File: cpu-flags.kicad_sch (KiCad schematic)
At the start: 10 parts, among them U44 74HCT02, U45 74HCT00, U9 74HCT173

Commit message: finished the control logic
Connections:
- no-connect marks 3 -> 5
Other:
- company: (none) -> TBR Designs
- title: (none) -> 8-bit CPU
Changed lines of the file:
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@@
 (kicad_sch (version 20230121) (generator eeschema)
   (paper "A4")
+  (title_block
+    (title "8-bit CPU")
+    (date "2023-11-28")
+    (rev "1.0")
+    (company "TBR Designs")
+  )
   (junction (at 135.89 132.08) (diameter 0) (color 0 0 0 0)
   )
@@
   (no_connect (at 201.93 100.33))
   (no_connect (at 199.39 100.33))
+  (no_connect (at 199.39 125.73))
+  (no_connect (at 201.93 125.73))
   (wire (pts (xy 142.24 87.63) (xy 181.61 87.63))
     (stroke (width 0) (type default) (color 255 0 0 1))

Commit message: redid the eeprom
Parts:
- renumbered D80 to D82, R127 to R125, U45 to U46, U44 to U47
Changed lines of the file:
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@@
   (symbol (lib_id "74xx:74HCT00") (at 125.73 95.25 0) (unit 3)
     (in_bom yes) (on_board yes) (dnp no) (fields_autoplaced)
-    (property "Reference" "U45" (at 125.7217 86.36 0)
+    (property "Reference" "U46" (at 125.7217 86.36 0)
       (effects (font (size 1.27 1.27)))
     )
@@
       (project "8-bit-cpu"
         (path "/100bb8d1-c3d6-4e1f-87b6-72e4e187243c/592ff0ed-0688-4db1-b04b-e905201025c7"
-          (reference "U45") (unit 3)
+          (reference "U46") (unit 3)
         )
       )
@@
   (symbol (lib_id "Device:R") (at 123.19 146.05 0) (unit 1)
     (in_bom yes) (on_board yes) (dnp no) (fields_autoplaced)
-    (property "Reference" "R127" (at 125.73 144.78 0)
+    (property "Reference" "R125" (at 125.73 144.78 0)
       (effects (font (size 1.27 1.27)) (justify left))
     )
@@
       (project "8-bit-cpu"
         (path "/100bb8d1-c3d6-4e1f-87b6-72e4e187243c/592ff0ed-0688-4db1-b04b-e905201025c7"
-          (reference "R127") (unit 1)
+          (reference "R125") (unit 1)
         )
       )
@@
         )
         (path "/100bb8d1-c3d6-4e1f-87b6-72e4e187243c/592ff0ed-0688-4db1-b04b-e905201025c7"
-          (reference "C53") (unit 1)
+          (reference "C54") (unit 1)
         )
       )
@@
         )
         (path "/100bb8d1-c3d6-4e1f-87b6-72e4e187243c/592ff0ed-0688-4db1-b04b-e905201025c7"
-          (reference "#PWR0191") (unit 1)
+          (reference "#PWR0189") (unit 1)
         )
       )
@@
   (symbol (lib_id "74xx:74HCT02") (at 67.31 72.39 0) (unit 1)
     (in_bom yes) (on_board yes) (dnp no) (fields_autoplaced)
-    (property "Reference" "U44" (at 67.31 63.5 0)
+    (property "Reference" "U47" (at 67.31 63.5 0)
       (effects (font (size 1.27 1.27)))
     )
@@
       (project "8-bit-cpu"
         (path "/100bb8d1-c3d6-4e1f-87b6-72e4e187243c/592ff0ed-0688-4db1-b04b-e905201025c7"
-          (reference "U44") (unit 1)
+          (reference "U47") (unit 1)
         )
       )
@@
         )
         (path "/100bb8d1-c3d6-4e1f-87b6-72e4e187243c/592ff0ed-0688-4db1-b04b-e905201025c7"
-          (reference "#PWR0194") (unit 1)
+          (reference "#PWR0192") (unit 1)
         )
       )
@@
   (symbol (lib_id "74xx:74HCT00") (at 237.49 41.91 0) (unit 5)
     (in_bom yes) (on_board yes) (dnp no) (fields_autoplaced)
-    (property "Reference" "U45" (at 243.84 40.64 0)
+    (property "Reference" "U46" (at 243.84 40.64 0)
       (effects (font (size 1.27 1.27)) (justify left))
     )
@@
       (project "8-bit-cpu"
         (path "/100bb8d1-c3d6-4e1f-87b6-72e4e187243c/592ff0ed-0688-4db1-b04b-e905201025c7"
-          (reference "U45") (unit 5)
+          (reference "U46") (unit 5)
         )
       )
@@
         )
         (path "/100bb8d1-c3d6-4e1f-87b6-72e4e187243c/592ff0ed-0688-4db1-b04b-e905201025c7"
-          (reference "#PWR0209") (unit 1)
+          (reference "#PWR0197") (unit 1)
         )
       )
@@
         )
         (path "/100bb8d1-c3d6-4e1f-87b6-72e4e187243c/592ff0ed-0688-4db1-b04b-e905201025c7"
-          (reference "#PWR0210") (unit 1)
+          (reference "#PWR0198") (unit 1)
         )
       )
@@
         )
         (path "/100bb8d1-c3d6-4e1f-87b6-72e4e187243c/592ff0ed-0688-4db1-b04b-e905201025c7"
-          (reference "C54") (unit 1)
+          (reference "C55") (unit 1)
         )
       )
@@
         )
         (path "/100bb8d1-c3d6-4e1f-87b6-72e4e187243c/592ff0ed-0688-4db1-b04b-e905201025c7"
-          (reference "#PWR0193") (unit 1)
+          (reference "#PWR0190") (unit 1)
         )
       )
@@
   (symbol (lib_id "Device:LED") (at 135.89 138.43 90) (unit 1)
     (in_bom yes) (on_board yes) (dnp no) (fields_autoplaced)
-    (property "Reference" "D80" (at 139.7 138.7475 90)
+    (property "Reference" "D82" (at 139.7 138.7475 90)
       (effects (font (size 1.27 1.27)) (justify right))
     )
@@
       (project "8-bit-cpu"
         (path "/100bb8d1-c3d6-4e1f-87b6-72e4e187243c/592ff0ed-0688-4db1-b04b-e905201025c7"
-          (reference "D80") (unit 1)
+          (reference "D82") (unit 1)
         )
       )
@@
   (symbol (lib_id "74xx:74HCT00") (at 96.52 80.01 0) (unit 1)
     (in_bom yes) (on_board yes) (dnp no) (fields_autoplaced)
-    (property "Reference" "U45" (at 96.5117 71.12 0)
+    (property "Reference" "U46" (at 96.5117 71.12 0)
       (effects (font (size 1.27 1.27)))
     )
@@
       (project "8-bit-cpu"
         (path "/100bb8d1-c3d6-4e1f-87b6-72e4e187243c/592ff0ed-0688-4db1-b04b-e905201025c7"
-          (reference "U45") (unit 1)
+          (reference "U46") (unit 1)
         )
       )
@@
         )
         (path "/100bb8d1-c3d6-4e1f-87b6-72e4e187243c/592ff0ed-0688-4db1-b04b-e905201025c7"
-          (reference "#PWR0196") (unit 1)
+          (reference "#PWR0195") (unit 1)
         )
       )
@@
         )
         (path "/100bb8d1-c3d6-4e1f-87b6-72e4e187243c/592ff0ed-0688-4db1-b04b-e905201025c7"
-          (reference "C58") (unit 1)
+          (reference "C56") (unit 1)
         )
       )
@@
   (symbol (lib_id "74xx:74HCT02") (at 67.31 87.63 0) (unit 2)
     (in_bom yes) (on_board yes) (dnp no) (fields_autoplaced)
-    (property "Reference" "U44" (at 67.31 78.74 0)
+    (property "Reference" "U47" (at 67.31 78.74 0)
       (effects (font (size 1.27 1.27)))
     )
@@
       (project "8-bit-cpu"
         (path "/100bb8d1-c3d6-4e1f-87b6-72e4e187243c/592ff0ed-0688-4db1-b04b-e905201025c7"
-          (reference "U44") (unit 2)
+          (reference "U47") (unit 2)
         )
       )
@@
   (symbol (lib_id "74xx:74HCT02") (at 67.31 102.87 0) (unit 3)
     (in_bom yes) (on_board yes) (dnp no) (fields_autoplaced)
-    (property "Reference" "U44" (at 67.31 93.98 0)
+    (property "Reference" "U47" (at 67.31 93.98 0)
       (effects (font (size 1.27 1.27)))
     )
@@
       (project "8-bit-cpu"
         (path "/100bb8d1-c3d6-4e1f-87b6-72e4e187243c/592ff0ed-0688-4db1-b04b-e905201025c7"
-          (reference "U44") (unit 3)
+          (reference "U47") (unit 3)
         )
       )
@@
         )
         (path "/100bb8d1-c3d6-4e1f-87b6-72e4e187243c/592ff0ed-0688-4db1-b04b-e905201025c7"
-          (reference "#PWR0195") (unit 1)
+          (reference "#PWR0194") (unit 1)
         )
       )
@@
   (symbol (lib_id "power:GND") (at 129.54 152.4 0) (unit 1)
     (in_bom yes) (on_board yes) (dnp no) (fields_autoplaced)
-    (property "Reference" "#PWR0190" (at 129.54 158.75 0)
+    (property "Reference" "#PWR0199" (at 129.54 158.75 0)
       (effects (font (size 1.27 1.27)) hide)
     )
@@
       (project "8-bit-cpu"
         (path "/100bb8d1-c3d6-4e1f-87b6-72e4e187243c/592ff0ed-0688-4db1-b04b-e905201025c7"
-          (reference "#PWR0190") (unit 1)
+          (reference "#PWR0199") (unit 1)
         )
       )
@@
         )
         (path "/100bb8d1-c3d6-4e1f-87b6-72e4e187243c/592ff0ed-0688-4db1-b04b-e905201025c7"
-          (reference "#PWR0192") (unit 1)
+          (reference "#PWR0191") (unit 1)
         )
       )
@@
   (symbol (lib_id "74xx:74HCT02") (at 265.43 41.91 0) (unit 5)
     (in_bom yes) (on_board yes) (dnp no) (fields_autoplaced)
-    (property "Reference" "U44" (at 271.78 40.64 0)
+    (property "Reference" "U47" (at 271.78 40.64 0)
       (effects (font (size 1.27 1.27)) (justify left))
     )
@@
       (project "8-bit-cpu"
         (path "/100bb8d1-c3d6-4e1f-87b6-72e4e187243c/592ff0ed-0688-4db1-b04b-e905201025c7"
-          (reference "U44") (unit 5)
+          (reference "U47") (unit 5)
         )
       )
@@
   (symbol (lib_id "74xx:74HCT00") (at 200.66 39.37 0) (unit 4)
     (in_bom yes) (on_board yes) (dnp no) (fields_autoplaced)
-    (property "Reference" "U45" (at 200.6517 30.48 0)
+    (property "Reference" "U46" (at 200.6517 30.48 0)
       (effects (font (size 1.27 1.27)))
     )
@@
       (project "8-bit-cpu"
         (path "/100bb8d1-c3d6-4e1f-87b6-72e4e187243c/592ff0ed-0688-4db1-b04b-e905201025c7"
-          (reference "U45") (unit 4)
+          (reference "U46") (unit 4)
         )
       )
@@
   (symbol (lib_id "74xx:74HCT00") (at 96.52 110.49 0) (unit 2)
     (in_bom yes) (on_board yes) (dnp no) (fields_autoplaced)
-    (property "Reference" "U45" (at 96.5117 101.6 0)
+    (property "Reference" "U46" (at 96.5117 101.6 0)
       (effects (font (size 1.27 1.27)))
     )
@@
       (project "8-bit-cpu"
         (path "/100bb8d1-c3d6-4e1f-87b6-72e4e187243c/592ff0ed-0688-4db1-b04b-e905201025c7"
-          (reference "U45") (unit 2)
+          (reference "U46") (unit 2)
         )
       )
@@
         )
         (path "/100bb8d1-c3d6-4e1f-87b6-72e4e187243c/592ff0ed-0688-4db1-b04b-e905201025c7"
-          (reference "U49") (unit 1)
+          (reference "U48") (unit 1)
         )
       )
@@
   (symbol (lib_id "74xx:74HCT02") (at 67.31 118.11 0) (unit 4)
     (in_bom yes) (on_board yes) (dnp no) (fields_autoplaced)
-    (property "Reference" "U44" (at 67.31 109.22 0)
+    (property "Reference" "U47" (at 67.31 109.22 0)
       (effects (font (size 1.27 1.27)))
     )
@@
       (project "8-bit-cpu"
         (path "/100bb8d1-c3d6-4e1f-87b6-72e4e187243c/592ff0ed-0688-4db1-b04b-e905201025c7"
-          (reference "U44") (unit 4)
+          (reference "U47") (unit 4)
         )
       )
@@
         )
         (path "/100bb8d1-c3d6-4e1f-87b6-72e4e187243c/592ff0ed-0688-4db1-b04b-e905201025c7"
-          (reference "#PWR0208") (unit 1)
+          (reference "#PWR0196") (unit 1)
         )
       )
@@
         )
         (path "/100bb8d1-c3d6-4e1f-87b6-72e4e187243c/592ff0ed-0688-4db1-b04b-e905201025c7"
-          (reference "#PWR0197") (unit 1)
-        )
-      )
+          (reference "#PWR0193") (unit 1)
+        )
+      )

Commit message: add pdf for instructions
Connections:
- net GND: now also U9.11 (D3), U9.12 (D2)
- no-connect marks 5 -> 3
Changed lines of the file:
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@@
   (junction (at 129.54 149.86) (diameter 0) (color 0 0 0 0)
+  )
+  (junction (at 194.31 97.79) (diameter 0) (color 0 0 0 0)
+  )
+  (junction (at 199.39 97.79) (diameter 0) (color 0 0 0 0)
   )
   (junction (at 184.15 100.33) (diameter 0) (color 255 0 0 1)
@@
   )
   (no_connect (at 208.28 39.37))
-  (no_connect (at 201.93 100.33))
-  (no_connect (at 199.39 100.33))
   (no_connect (at 199.39 125.73))
   (no_connect (at 201.93 125.73))
+  (wire (pts (xy 194.31 97.79) (xy 199.39 97.79))
+    (stroke (width 0) (type default))
+  )
   (wire (pts (xy 142.24 87.63) (xy 181.61 87.63))
     (stroke (width 0) (type default) (color 255 0 0 1))
@@
     (stroke (width 0) (type default))
   )
+  (wire (pts (xy 199.39 97.79) (xy 199.39 100.33))
+    (stroke (width 0) (type default))
+  )
   (wire (pts (xy 45.72 86.36) (xy 50.8 86.36))
     (stroke (width 0) (type default))
@@
     (stroke (width 0) (type default))
   )
-  (wire (pts (xy 194.31 97.79) (xy 191.77 97.79))
+  (wire (pts (xy 191.77 97.79) (xy 194.31 97.79))
     (stroke (width 0) (type default))
   )
@@
   )
   (wire (pts (xy 135.89 134.62) (xy 135.89 132.08))
+    (stroke (width 0) (type default))
+  )
+  (wire (pts (xy 201.93 100.33) (xy 201.93 97.79))
     (stroke (width 0) (type default))
   )
@@
     (stroke (width 0) (type default))
   )
+  (wire (pts (xy 199.39 97.79) (xy 201.93 97.79))
+    (stroke (width 0) (type default))
+  )

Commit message: fixed gate type in cpu flags
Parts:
- removed U46: 74HCT00, symbol 74xx:74HCT00
- added U42: 74HCT08, symbol 74xx:74LS08
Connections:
- net +5V: now also U42.14 (VCC)
- net GND: now also U42.12, U42.13, U42.7 (GND)
- net at U9.13 (D1): now also U42.8
- net at U47.1: now also U42.1
- net at U47.4: now also U42.2
- net at U47.10: now also U42.4
- net at U47.13: now also U42.5
- new net: U42.10, U42.6
- new net: U42.3, U42.9

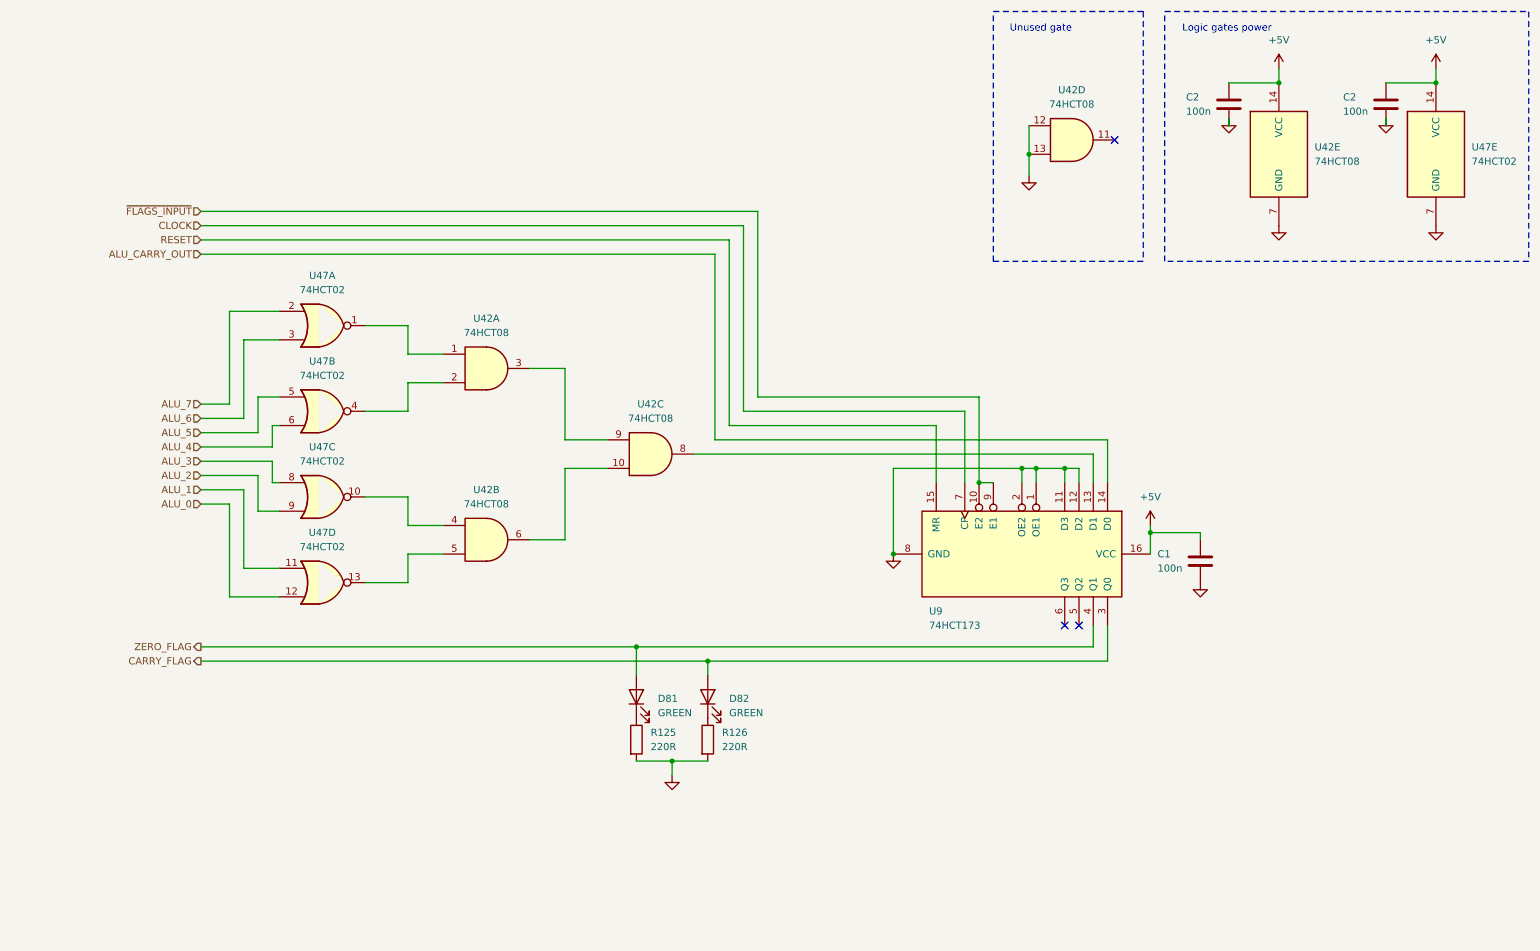
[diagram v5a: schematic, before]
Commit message: added stack and x register.  Added logic for stack_address so ram address 7 gets passes and ram address 8 is high
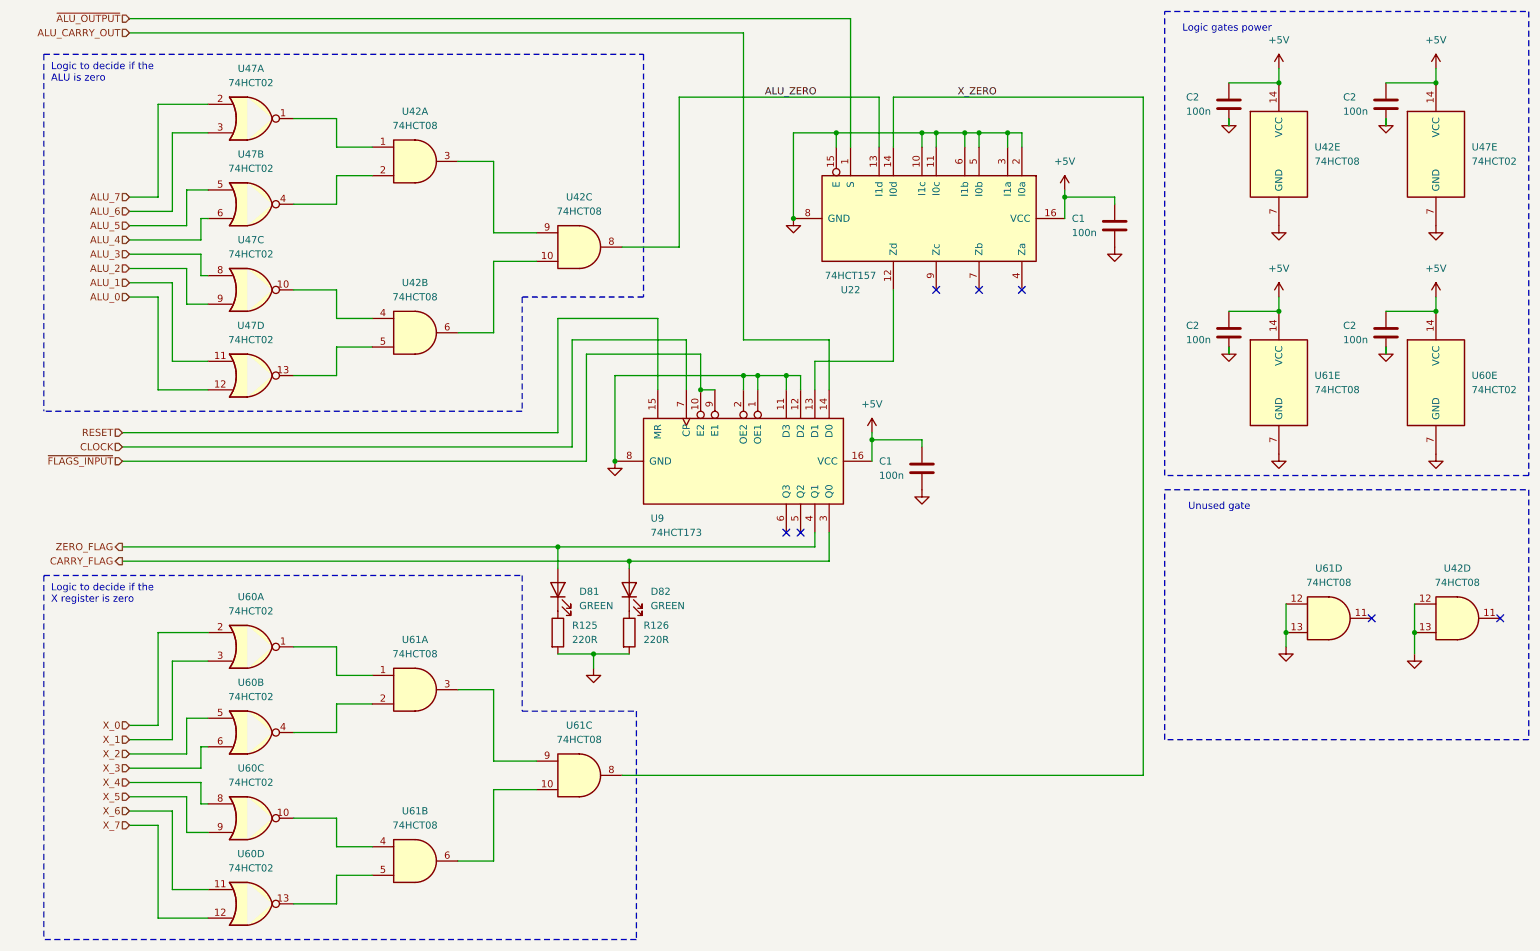
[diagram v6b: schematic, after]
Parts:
- added C1, C2 (x2): 100n, 01_my_library:C_Disc_D4.0mm_W2.6mm_P2.50mm, symbol Device:C
- added U22: 74HCT157, Package_DIP:DIP-16_W7.62mm, symbol 74xx:74LS157
- added U60: 74HCT02, symbol 74xx:74HCT02
- added U61: 74HCT08, symbol 74xx:74LS08
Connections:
- net +5V: now also C1.1, C2.1, C2.1, U22.16 (VCC), U60.14 (VCC), U61.14 (VCC)
- net GND: now also C1.2, C2.2, C2.2, U22.10 (I1c), U22.11 (I0c), U22.15 (E), U22.2 (I0a), U22.3 (I1a), U22.5 (I0b), U22.6 (I1b), U22.8 (GND), U60.7 (GND), U61.12, U61.13, U61.7 (GND)
- net at U9.13 (D1): now also U22.12 (Zd); no longer U42.8
- new net: U60.1, U61.1
- new net: U60.4, U61.2
- new net: U60.13, U61.5
- new net: U61.3, U61.9
- new net: U61.10, U61.6
- new net: U60.10, U61.4
- new net ALU_ZERO: U22.13 (I1d), U42.8
- new net X_0: U60.2
- new net X_1: U60.3
- new net X_2: U60.5
- new net X_3: U60.6
- new net X_4: U60.8
- new net X_5: U60.9
- new net X_6: U60.11
- new net X_7: U60.12
- new net X_ZERO: U22.14 (I0d), U61.8
- new net ~{ALU_OUTPUT}: U22.1 (S)
- no-connect marks 3 -> 7
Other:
- note added: "Logic to decide if the ALU is zero"
- note added: "Logic to decide if the X register is zero"
- moved on the sheet: C1, D81, D82, R125, R126, U42A, U42B, U42C, U42D, U47A, U47B, U47C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

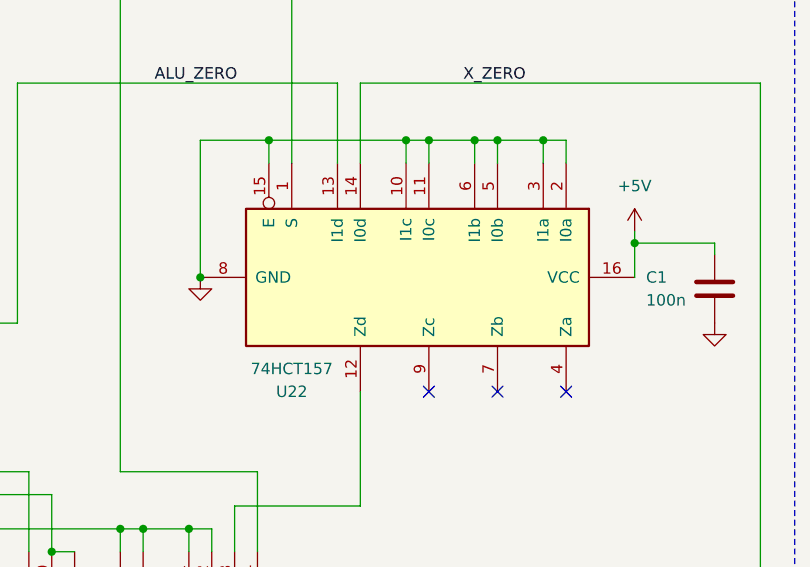
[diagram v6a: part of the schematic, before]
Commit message: changed symbols
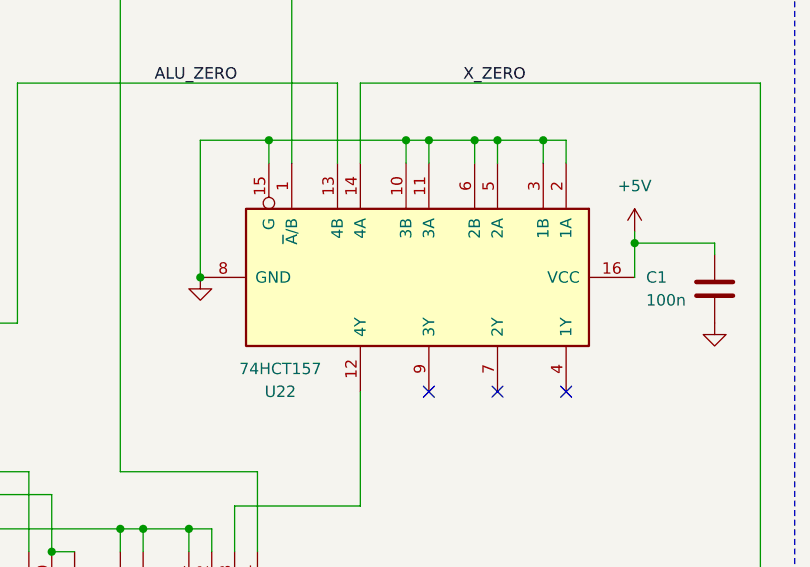
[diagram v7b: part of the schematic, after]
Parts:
- U22: symbol 74xx:74LS157 -> 01_my_library:74HCT157
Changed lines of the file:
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@@
     )
   )
-  (symbol (lib_id "74xx:74LS157") (at 176.53 53.34 270) (unit 1)
+  (symbol (lib_id "01_my_library:74HCT157") (at 175.26 53.34 270) (unit 1)
     (in_bom yes) (on_board yes) (dnp no)
-    (property "Reference" "U22" (at 161.29 66.04 90)
+    (property "Reference" "U22" (at 160.02 66.04 90)
       (effects (font (size 1.27 1.27)))
     )
-    (property "Value" "74HCT157" (at 161.29 63.5 90)
+    (property "Value" "74HCT157" (at 160.02 63.5 90)
       (effects (font (size 1.27 1.27)))
     )
-    (property "Footprint" "Package_DIP:DIP-16_W7.62mm" (at 176.53 53.34 0)
+    (property "Footprint" "Package_DIP:DIP-16_W7.62mm" (at 175.26 54.61 0)
       (effects (font (size 1.27 1.27)) hide)
     )
-    (property "Datasheet" "http://www.ti.com/lit/gpn/sn74LS157" (at 176.53 53.34 0)
+    (property "Datasheet" "https://www.ti.com/lit/ds/symlink/sn74hct157.pdf" (at 139.7 54.61 0)
       (effects (font (size 1.27 1.27)) hide)
     )

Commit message: some cleanup
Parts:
- renumbered D81 to D106, D82 to D107, R125 to R150, R126 to R151, U47 to U50, U42 to U51, U61 to U53, U60 to U54
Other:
- moved on the sheet: U51D, U53D
